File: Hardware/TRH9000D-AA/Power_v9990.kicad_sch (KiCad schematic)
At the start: 41 parts, among them U1 V9990, U2 KM428C256, U3 KM428C256, U4 74VHC138, U5 T.I_SN74AHCT32D, U6 LMH1980, U7 T.I_SN74CBT3257, U8 LMH1980, U9 SST39SF010A-lrj

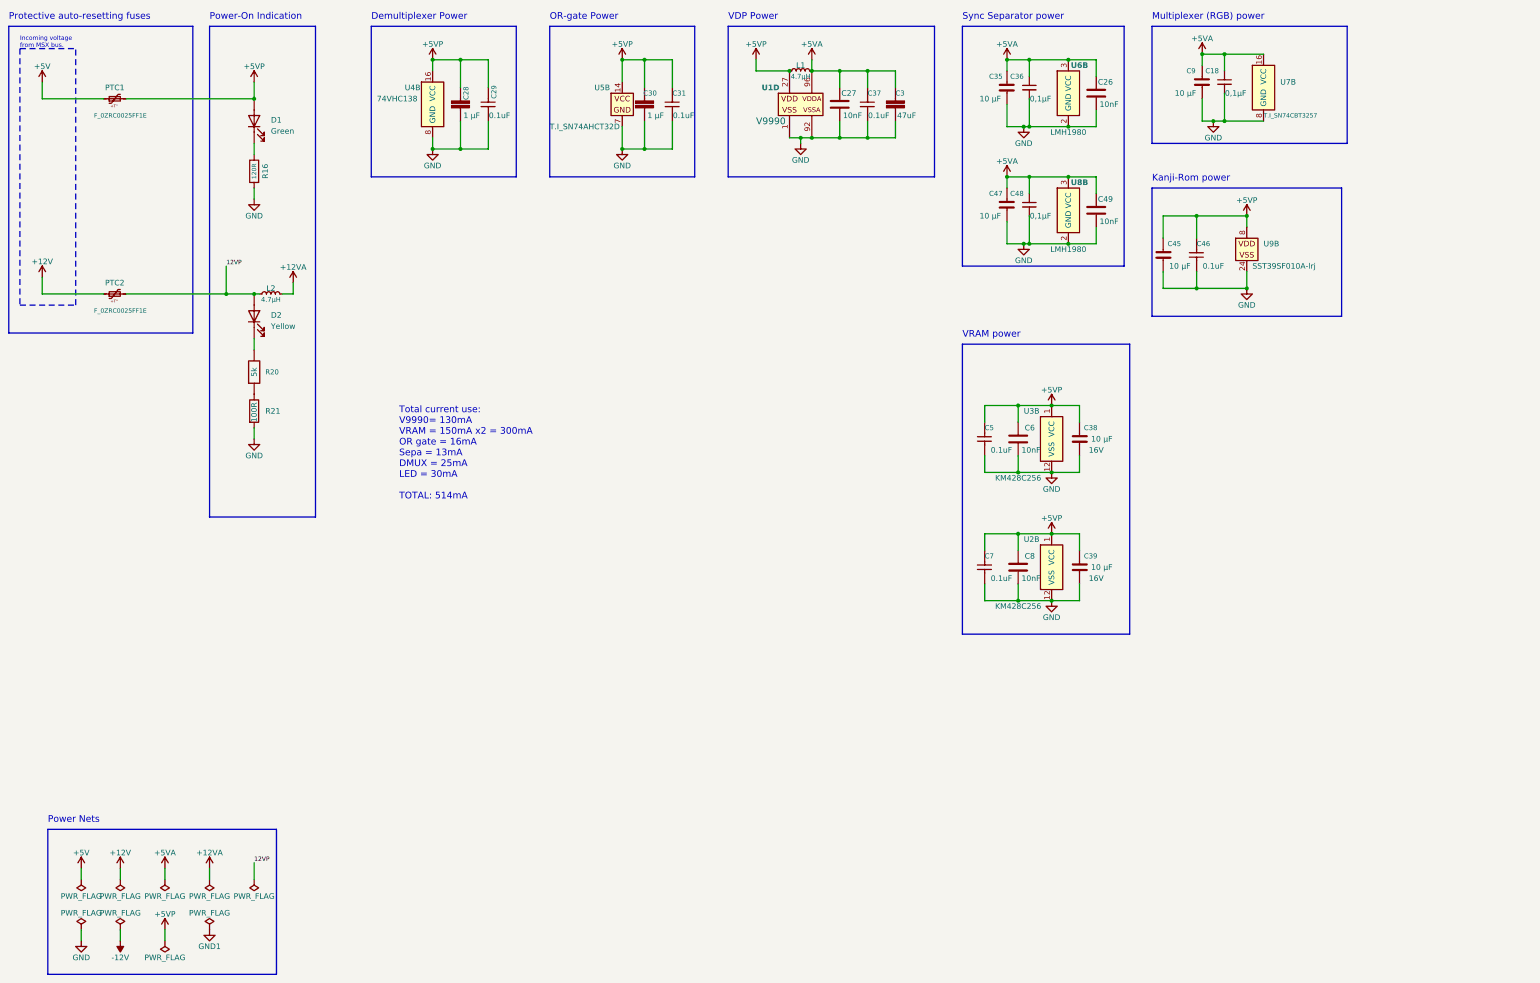
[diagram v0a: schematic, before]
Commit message: Finished rerouting the AA-variant, and replaced the fuses with SMD-ones.
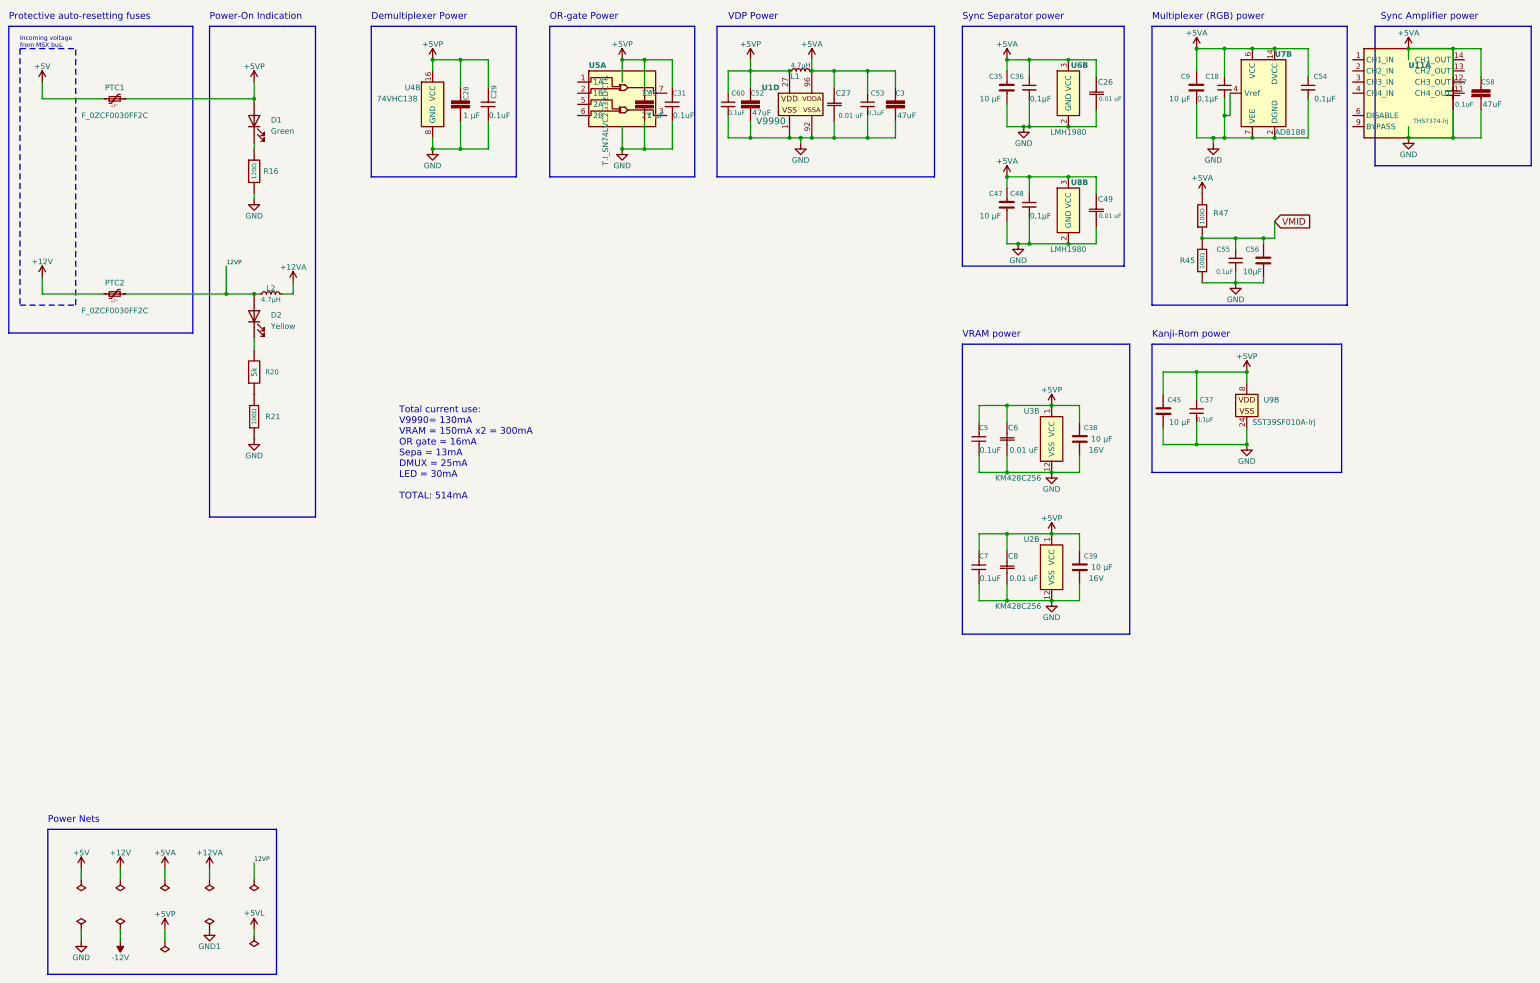
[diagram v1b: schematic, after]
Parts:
- removed C37, C46: C_CC0805JPX7R9BB104, Capacitor_SMD:C_0805_2012Metric, symbol LRJ-parts:C_CC0805JPX7R9BB104
- removed U5: T.I_SN74AHCT32D, trh9000:Texas_R-PDSO-G14_3.6x4.4mm, symbol TRH9000:T.I_SN74AHCT32D
- added C37, C53, C54, C55, C60: C_CL10B104KB8NNNL, Capacitor_SMD:C_0603_1608Metric_Pad1.08x0.95mm_HandSolder, symbol LRJ-parts:C_CL10B104KB8NNNL
- added C52, C58: C_GRM21BR61A476ME15K, Capacitor_SMD:C_0805_2012Metric, symbol LRJ-parts:C_GRM21BR61A476ME15K
- added C56: C_CL21B106KOQNNNE, Capacitor_SMD:C_0805_2012Metric, symbol LRJ-parts:C_CL21B106KOQNNNE
- added C57: C_CC0805JPX7R9BB104, Capacitor_SMD:C_0805_2012Metric, symbol LRJ-parts:C_CC0805JPX7R9BB104
- added R45, R47: R_CRGP0603F220R, Resistor_SMD:R_0603_1608Metric, symbol LRJ-parts:R_CRG0603F100R
- added U11: THS7374-lrj, Package_SO:TSSOP-14_4.4x5mm_P0.65mm, symbol LRJ-parts:THS7374-lrj
- added U5: T.I_SN74LVC2G32DCTR, Package_SO:SSOP-8_2.95x2.8mm_P0.65mm, symbol TRH9000:T.I_SN74LVC2G32DCTR
- C18, C36, C48: Mounting type (none) -> SMD
- C26, C27, C49, C6, C8: value 10nF -> C_CL21B103KBANNNC; symbol Device:C -> LRJ-parts:C_CL21B103KBANNNC; Capacitance (none) -> 0.01 uF; MPN (none) -> CL21B103KBANNNC; Manufacturer (none) -> Samsung Electro-Mechanics; Mounting type (none) -> SMD; Mouser datasheet (none) -> https://www.mouser.se/datasheet/2/427/vjcommercialseries-17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; Price (none) -> €0,08; Status (none) -> Active; Temperature Coefficient  (none) -> X7R; Voltage rating (none) -> 50V
- PTC1, PTC2: value F_0ZRC0025FF1E -> F_0ZCF0030FF2C; footprint LRJ:Fuse_BelFuse_0ZRC0025FF_L7.4mm_W3.1mm -> Fuse:Fuse_2920_7451Metric; symbol LRJ-parts:F_0ZRC0025FF1E -> LRJ-parts:F_0ZCF0030FF2C; Current Rating 40A -> 100A; Ih 250mA -> 300mA; It 500mA -> 600mA; MPN 0ZRC0025FF1E -> 0ZCF0030FF2C; Mounting type THT -> SMD; Mouser datasheet https://www.mouser.se/datasheet/2/643/ds_CP_0zrc_series-196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 -> (none); Mouser detail page https://www.mouser.se/ProductDetail/Bel-Fuse/0ZRR0025FF1E?q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 -> (none); Price 0,25€ -> (none); Ri (min) 1,25 Ohms -> 1 Ohms; Time to Trip  2.5s -> 3s; Voltage Rating (none) -> 60V
- R16: value 120R -> R_ERJ-3EKF10R0V; symbol Device:R -> LRJ-parts:R_ERJ-3EKF1200V; Details (none) -> https://industrial.panasonic.com/ww/products/pt/general-pur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; MPN (none) -> ERJ-3EKF10R0V; Manufacturer (none) -> Panasonic; Operating temperature (none) -> -55C to +155C; Resistance (none) -> 120Ω; Status (none) -> Active; Tolerance (none) -> ±1%; Voltage rating (none) -> 75V
- R21: value 100R -> R_CRGP0603F220R; footprint Resistor_SMD:R_0805_2012Metric -> Resistor_SMD:R_0603_1608Metric; symbol Device:R -> LRJ-parts:R_CRG0603F100R; MPN (none) -> CRGP0603F220R; Manufacturer (none) -> TE Connectivity; Operating Temperature  (none) -> -55°C to 125°C; Power (Watts)  (none) -> 0.1W, 1/10W; Resistance (none) -> 100Ω; Status (none) -> Active
- U7: value T.I_SN74CBT3257 -> AD8188; footprint trh9000:Texas_R-PDSO-G16_3.9x9.9mm -> Package_SO:TSSOP-24_4.4x7.8mm_P0.65mm; symbol TRH9000:T.I_SN74CBT3257 -> LRJ-parts:AD8188; MPN SN74CBT3257DR -> AD8188ARUZ; Manufacturer Texas Instruments -> Analog Devices Inc.
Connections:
- net +5VA: now also U7.13 (VCC), U7.14 (DVCC), U7.17 (VCC), U7.21 (VCC), U7.24 (VCC), U7.6 (VCC), C53.1, C54.1, C57.1, C58.1, R47.1; no longer U7.16 (VCC)
- net +5VP: now also C37.1, C52.1, C60.1
- net GND: now also U7.11 (VEE), U7.15 (VEE), U7.19 (VEE), U7.2 (DGND), U7.4 (Vref), U7.7 (VEE), U7.9 (VEE), C37.2, C52.2, C53.2, C54.2, C55.2, C56.2, C57.2, C58.2, C60.2, R45.2; no longer U7.8 (GND)
- new net VMID: C55.1, C56.1, R45.1, R47.2
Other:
- note added: "Sync Amplifier power"
- moved on the sheet: C18, C45, C5, C7, C9, R16, R21, U9B
